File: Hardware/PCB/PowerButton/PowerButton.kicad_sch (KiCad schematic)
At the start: 12 parts, among them J1 Conn_01x07_Pin, Q24 2N3904, Q25 2N3904, Q26 2N3904, Q27 2N3904, Q28 P-Channel MOSFET

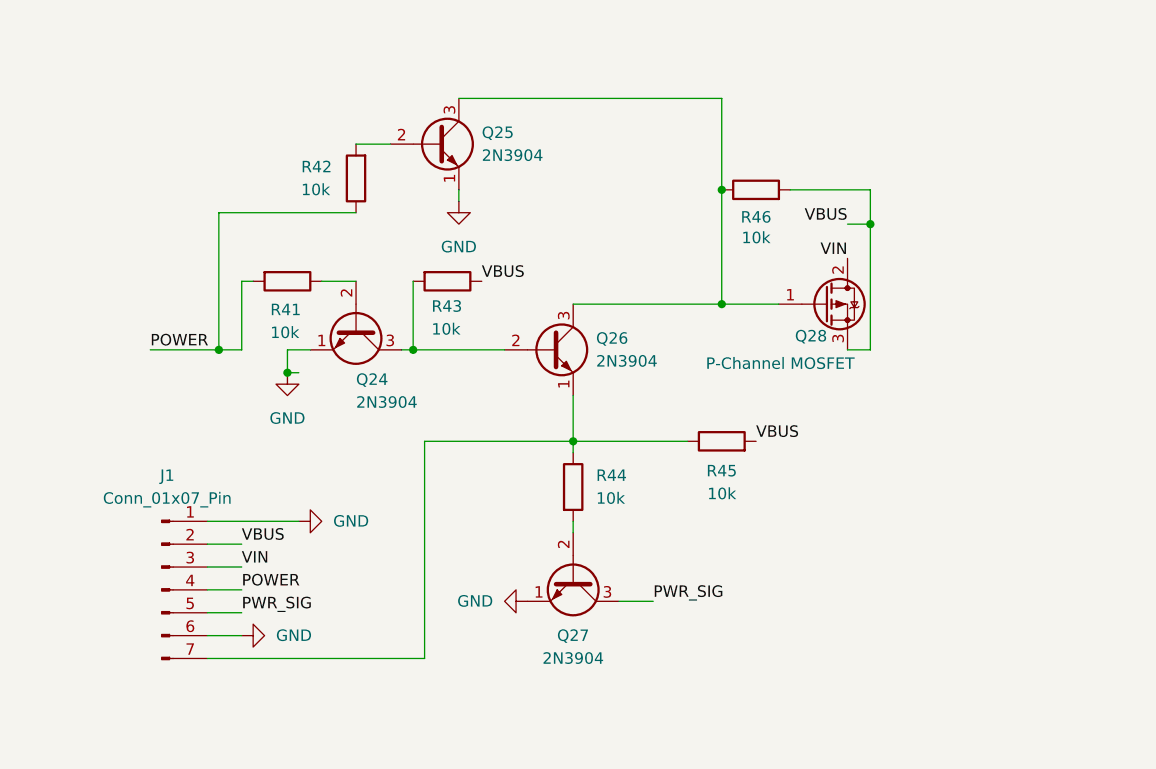
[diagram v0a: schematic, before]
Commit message: Fix 3D model exporting problem
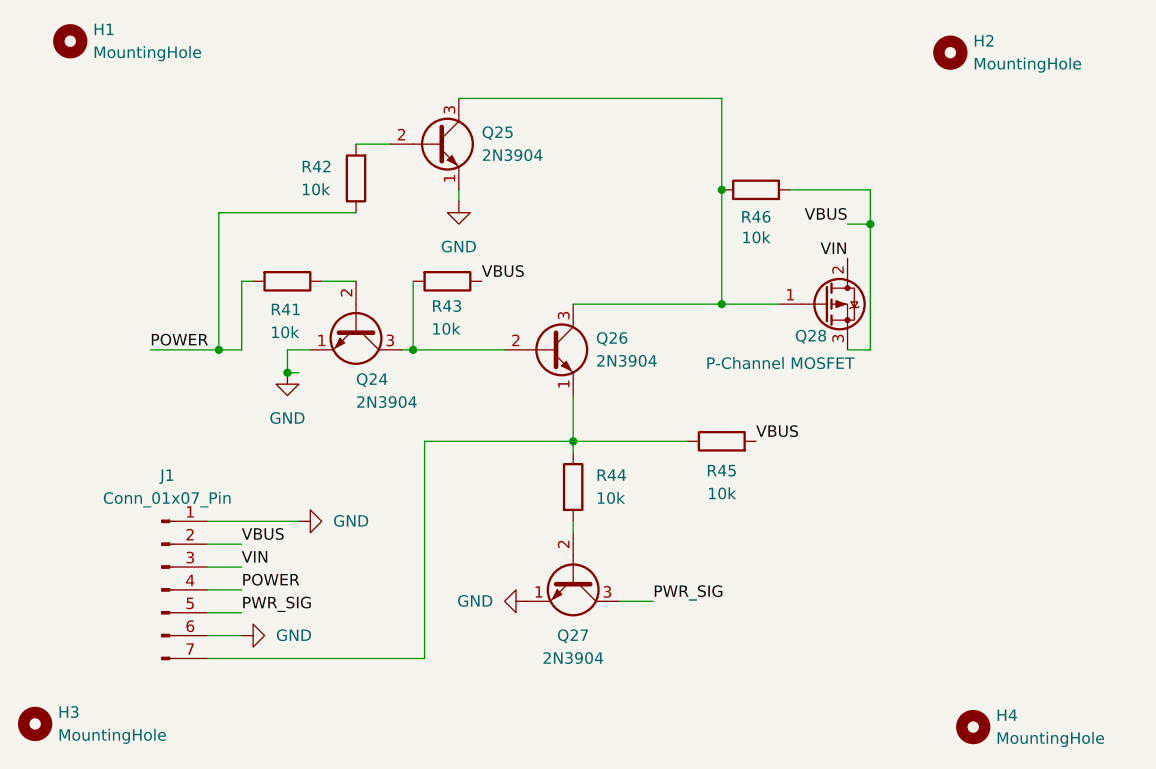
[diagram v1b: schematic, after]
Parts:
- added H1, H2, H3, H4: MountingHole, MountingHole:MountingHole_2.2mm_M2, symbol Mechanical:MountingHole

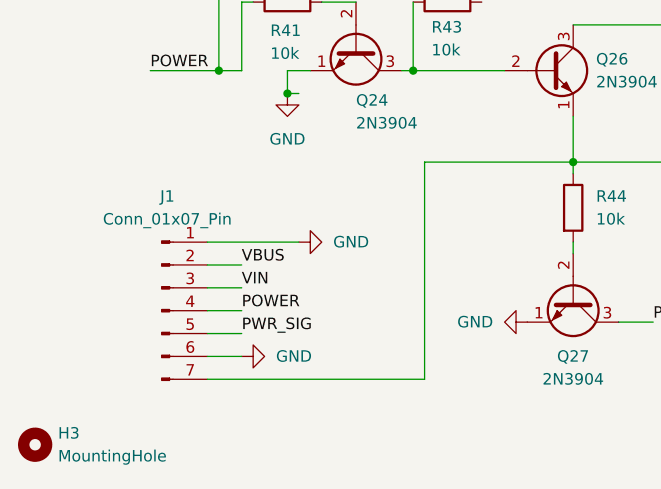
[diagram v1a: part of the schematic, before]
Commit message: Push before system switch - my arch crashed, have tgo switch to windows now
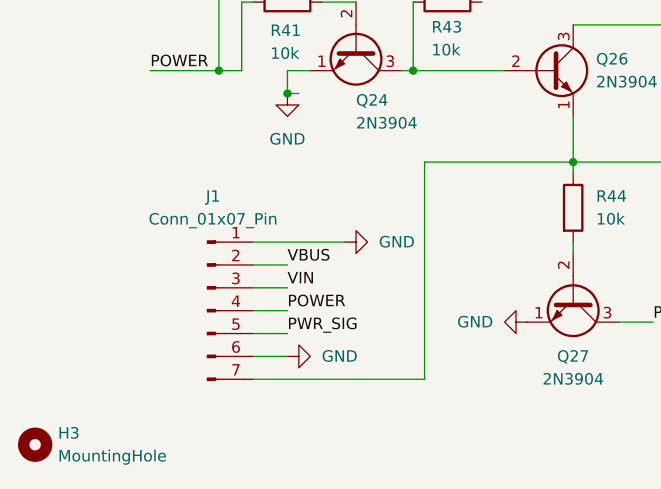
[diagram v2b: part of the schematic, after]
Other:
- moved on the sheet: J1
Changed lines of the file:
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@@
 	(wire
 		(pts
-			(xy 96.52 104.14) (xy 100.33 104.14)
+			(xy 101.6 104.14) (xy 105.41 104.14)
 		)
 		(stroke
@@
 	(wire
 		(pts
-			(xy 96.52 106.68) (xy 120.65 106.68)
+			(xy 101.6 106.68) (xy 120.65 106.68)
 		)
 		(stroke
@@
 	(wire
 		(pts
-			(xy 96.52 96.52) (xy 100.33 96.52)
+			(xy 101.6 96.52) (xy 105.41 96.52)
 		)
 		(stroke
@@
 	(wire
 		(pts
-			(xy 96.52 99.06) (xy 100.33 99.06)
+			(xy 101.6 99.06) (xy 105.41 99.06)
 		)
 		(stroke
@@
 	(wire
 		(pts
-			(xy 96.52 101.6) (xy 100.33 101.6)
+			(xy 101.6 101.6) (xy 105.41 101.6)
 		)
 		(stroke
@@
 	(wire
 		(pts
-			(xy 96.52 91.44) (xy 106.68 91.44)
-		)
-		(stroke
-			(width 0)
-			(type default)
-		)
-	)
-	(wire
-		(pts
-			(xy 96.52 93.98) (xy 100.33 93.98)
+			(xy 101.6 91.44) (xy 111.76 91.44)
+		)
+		(stroke
+			(width 0)
+			(type default)
+		)
+	)
+	(wire
+		(pts
+			(xy 101.6 93.98) (xy 105.41 93.98)
 		)
 		(stroke
@@
 	)
 	(label "POWER"
-		(at 100.33 99.06 0)
+		(at 105.41 99.06 0)
 		(effects
 			(font
@@
 	)
 	(label "PWR_SIG"
-		(at 100.33 101.6 0)
+		(at 105.41 101.6 0)
 		(effects
 			(font
@@
 	)
 	(label "VIN"
-		(at 100.33 96.52 0)
+		(at 105.41 96.52 0)
 		(effects
 			(font
@@
 	)
 	(label "VBUS"
-		(at 100.33 93.98 0)
+		(at 105.41 93.98 0)
 		(effects
 			(font
@@
 	(symbol
 		(lib_id "power:GND")
-		(at 100.33 104.14 90)
+		(at 105.41 104.14 90)
 		(unit 1)
 		(body_style 1)
@@
 		(fields_autoplaced yes)
 		(property "Reference" "#PWR02"
-			(at 106.68 104.14 0)
+			(at 111.76 104.14 0)
 			(hide yes)
 			(show_name no)
@@
 		)
 		(property "Value" "GND"
-			(at 104.14 104.1399 90)
+			(at 109.22 104.1399 90)
 			(show_name no)
 			(do_not_autoplace no)
@@
 		)
 		(property "Footprint" ""
-			(at 100.33 104.14 0)
+			(at 105.41 104.14 0)
 			(hide yes)
 			(show_name no)
@@
 		)
 		(property "Datasheet" ""
-			(at 100.33 104.14 0)
+			(at 105.41 104.14 0)
 			(hide yes)
 			(show_name no)
@@
 		)
 		(property "Description" "Power symbol creates a global label with name \"GND\" , ground"
-			(at 100.33 104.14 0)
+			(at 105.41 104.14 0)
 			(hide yes)
 			(show_name no)
@@
 	(symbol
 		(lib_id "Connector:Conn_01x07_Pin")
-		(at 91.44 99.06 0)
+		(at 96.52 99.06 0)
 		(unit 1)
 		(body_style 1)
@@
 		(fields_autoplaced yes)
 		(property "Reference" "J1"
-			(at 92.075 86.36 0)
+			(at 97.155 86.36 0)
 			(show_name no)
 			(do_not_autoplace no)
@@
 		)
 		(property "Value" "Conn_01x07_Pin"
-			(at 92.075 88.9 0)
+			(at 97.155 88.9 0)
 			(show_name no)
 			(do_not_autoplace no)
@@
 		)
 		(property "Footprint" "Connector_PinHeader_2.54mm:PinHeader_1x07_P2.54mm_Vertical"
-			(at 91.44 99.06 0)
+			(at 96.52 99.06 0)
 			(hide yes)
 			(show_name no)
@@
 		)
 		(property "Datasheet" ""
-			(at 91.44 99.06 0)
+			(at 96.52 99.06 0)
 			(hide yes)
 			(show_name no)
@@
 		)
 		(property "Description" "Generic connector, single row, 01x07, script generated"
-			(at 91.44 99.06 0)
+			(at 96.52 99.06 0)
 			(hide yes)
 			(show_name no)
@@
 	(symbol
 		(lib_id "power:GND")
-		(at 106.68 91.44 90)
+		(at 111.76 91.44 90)
 		(unit 1)
 		(body_style 1)
@@
 		(fields_autoplaced yes)
 		(property "Reference" "#PWR01"
-			(at 113.03 91.44 0)
+			(at 118.11 91.44 0)
 			(hide yes)
 			(show_name no)
@@
 		)
 		(property "Value" "GND"
-			(at 110.49 91.4399 90)
+			(at 115.57 91.4399 90)
 			(show_name no)
 			(do_not_autoplace no)
@@
 		)
 		(property "Footprint" ""
-			(at 106.68 91.44 0)
+			(at 111.76 91.44 0)
 			(hide yes)
 			(show_name no)
@@
 		)
 		(property "Datasheet" ""
-			(at 106.68 91.44 0)
+			(at 111.76 91.44 0)
 			(hide yes)
 			(show_name no)
@@
 		)
 		(property "Description" "Power symbol creates a global label with name \"GND\" , ground"
-			(at 106.68 91.44 0)
-			(hide yes)
-			(show_name no)
+			(at 111.76 91.44 0)
+			(hide yes)
+			(show_name no)
